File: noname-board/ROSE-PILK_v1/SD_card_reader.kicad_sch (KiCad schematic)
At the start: 1 part, among them J5 Conn_02x08_Odd_Even

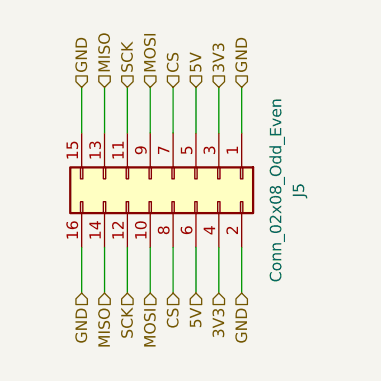
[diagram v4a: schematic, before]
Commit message: schematic finished, placement progress
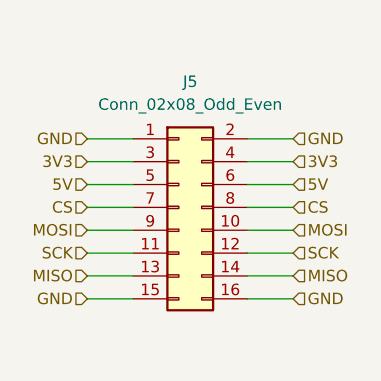
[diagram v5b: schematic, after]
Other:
- moved on the sheet: J5
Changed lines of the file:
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@@
 (kicad_sch (version 20230121) (generator eeschema)
   (paper "A4")
-  (wire (pts (xy 126.365 130.175) (xy 126.365 135.255))
+  (wire (pts (xy 129.54 120.65) (xy 134.62 120.65))
     (stroke (width 0) (type default))
   )
-  (wire (pts (xy 123.825 112.395) (xy 123.825 117.475))
+  (wire (pts (xy 111.76 123.19) (xy 116.84 123.19))
     (stroke (width 0) (type default))
   )
-  (wire (pts (xy 128.905 130.175) (xy 128.905 135.255))
+  (wire (pts (xy 129.54 118.11) (xy 134.62 118.11))
     (stroke (width 0) (type default))
   )
-  (wire (pts (xy 123.825 130.175) (xy 123.825 135.255))
+  (wire (pts (xy 129.54 123.19) (xy 134.62 123.19))
     (stroke (width 0) (type default))
   )
-  (wire (pts (xy 113.665 130.175) (xy 113.665 135.255))
+  (wire (pts (xy 129.54 133.35) (xy 134.62 133.35))
     (stroke (width 0) (type default))
   )
-  (wire (pts (xy 116.205 112.395) (xy 116.205 117.475))
+  (wire (pts (xy 111.76 130.81) (xy 116.84 130.81))
     (stroke (width 0) (type default))
   )
-  (wire (pts (xy 121.285 130.175) (xy 121.285 135.255))
+  (wire (pts (xy 129.54 125.73) (xy 134.62 125.73))
     (stroke (width 0) (type default))
   )
-  (wire (pts (xy 116.205 130.175) (xy 116.205 135.255))
+  (wire (pts (xy 129.54 130.81) (xy 134.62 130.81))
     (stroke (width 0) (type default))
   )
-  (wire (pts (xy 118.745 130.175) (xy 118.745 135.255))
+  (wire (pts (xy 129.54 128.27) (xy 134.62 128.27))
     (stroke (width 0) (type default))
   )
-  (wire (pts (xy 111.125 130.175) (xy 111.125 135.255))
+  (wire (pts (xy 129.54 135.89) (xy 134.62 135.89))
     (stroke (width 0) (type default))
   )
-  (wire (pts (xy 113.665 112.395) (xy 113.665 117.475))
+  (wire (pts (xy 111.76 133.35) (xy 116.84 133.35))
     (stroke (width 0) (type default))
   )
-  (wire (pts (xy 118.745 112.395) (xy 118.745 117.475))
+  (wire (pts (xy 111.76 128.27) (xy 116.84 128.27))
     (stroke (width 0) (type default))
   )
-  (wire (pts (xy 128.905 112.395) (xy 128.905 117.475))
+  (wire (pts (xy 111.76 118.11) (xy 116.84 118.11))
     (stroke (width 0) (type default))
   )
-  (wire (pts (xy 121.285 112.395) (xy 121.285 117.475))
+  (wire (pts (xy 111.76 125.73) (xy 116.84 125.73))
     (stroke (width 0) (type default))
   )
-  (wire (pts (xy 126.365 112.395) (xy 126.365 117.475))
+  (wire (pts (xy 111.76 120.65) (xy 116.84 120.65))
     (stroke (width 0) (type default))
   )
-  (wire (pts (xy 111.125 112.395) (xy 111.125 117.475))
+  (wire (pts (xy 111.76 135.89) (xy 116.84 135.89))
     (stroke (width 0) (type default))
   )
-  (hierarchical_label "GND" (shape input) (at 111.125 112.395 90) (fields_autoplaced)
+  (hierarchical_label "GND" (shape input) (at 111.76 135.89 180) (fields_autoplaced)
+    (effects (font (size 1.27 1.27)) (justify right))
+  )
+  (hierarchical_label "GND" (shape input) (at 134.62 135.89 0) (fields_autoplaced)
     (effects (font (size 1.27 1.27)) (justify left))
   )
-  (hierarchical_label "GND" (shape input) (at 111.125 135.255 270) (fields_autoplaced)
+  (hierarchical_label "MISO" (shape input) (at 134.62 133.35 0) (fields_autoplaced)
+    (effects (font (size 1.27 1.27)) (justify left))
+  )
+  (hierarchical_label "MOSI" (shape input) (at 134.62 128.27 0) (fields_autoplaced)
+    (effects (font (size 1.27 1.27)) (justify left))
+  )
+  (hierarchical_label "SCK" (shape input) (at 134.62 130.81 0) (fields_autoplaced)
+    (effects (font (size 1.27 1.27)) (justify left))
+  )
+  (hierarchical_label "GND" (shape input) (at 111.76 118.11 180) (fields_autoplaced)
     (effects (font (size 1.27 1.27)) (justify right))
   )
-  (hierarchical_label "MISO" (shape input) (at 113.665 135.255 270) (fields_autoplaced)
+  (hierarchical_label "SCK" (shape input) (at 111.76 130.81 180) (fields_autoplaced)
     (effects (font (size 1.27 1.27)) (justify right))
   )
-  (hierarchical_label "MOSI" (shape input) (at 118.745 135.255 270) (fields_autoplaced)
+  (hierarchical_label "MISO" (shape input) (at 111.76 133.35 180) (fields_autoplaced)
     (effects (font (size 1.27 1.27)) (justify right))
   )
-  (hierarchical_label "SCK" (shape input) (at 116.205 135.255 270) (fields_autoplaced)
+  (hierarchical_label "3V3" (shape input) (at 134.62 120.65 0) (fields_autoplaced)
+    (effects (font (size 1.27 1.27)) (justify left))
+  )
+  (hierarchical_label "3V3" (shape input) (at 111.76 120.65 180) (fields_autoplaced)
     (effects (font (size 1.27 1.27)) (justify right))
   )
-  (hierarchical_label "GND" (shape input) (at 128.905 112.395 90) (fields_autoplaced)
+  (hierarchical_label "GND" (shape input) (at 134.62 118.11 0) (fields_autoplaced)
     (effects (font (size 1.27 1.27)) (justify left))
   )
-  (hierarchical_label "SCK" (shape input) (at 116.205 112.395 90) (fields_autoplaced)
+  (hierarchical_label "CS" (shape input) (at 111.76 125.73 180) (fields_autoplaced)
+    (effects (font (size 1.27 1.27)) (justify right))
+  )
+  (hierarchical_label "5V" (shape input) (at 134.62 123.19 0) (fields_autoplaced)
     (effects (font (size 1.27 1.27)) (justify left))
   )
-  (hierarchical_label "MISO" (shape input) (at 113.665 112.395 90) (fields_autoplaced)
+  (hierarchical_label "5V" (shape input) (at 111.76 123.19 180) (fields_autoplaced)
+    (effects (font (size 1.27 1.27)) (justify right))
+  )
+  (hierarchical_label "CS" (shape input) (at 134.62 125.73 0) (fields_autoplaced)
     (effects (font (size 1.27 1.27)) (justify left))
   )
-  (hierarchical_label "3V3" (shape input) (at 126.365 135.255 270) (fields_autoplaced)
+  (hierarchical_label "MOSI" (shape input) (at 111.76 128.27 180) (fields_autoplaced)
     (effects (font (size 1.27 1.27)) (justify right))
   )
-  (hierarchical_label "3V3" (shape input) (at 126.365 112.395 90) (fields_autoplaced)
-    (effects (font (size 1.27 1.27)) (justify left))
-  )
-  (hierarchical_label "GND" (shape input) (at 128.905 135.255 270) (fields_autoplaced)
-    (effects (font (size 1.27 1.27)) (justify right))
-  )
-  (hierarchical_label "CS" (shape input) (at 121.285 112.395 90) (fields_autoplaced)
-    (effects (font (size 1.27 1.27)) (justify left))
-  )
-  (hierarchical_label "5V" (shape input) (at 123.825 135.255 270) (fields_autoplaced)
-    (effects (font (size 1.27 1.27)) (justify right))
-  )
-  (hierarchical_label "5V" (shape input) (at 123.825 112.395 90) (fields_autoplaced)
-    (effects (font (size 1.27 1.27)) (justify left))
-  )
-  (hierarchical_label "CS" (shape input) (at 121.285 135.255 270) (fields_autoplaced)
-    (effects (font (size 1.27 1.27)) (justify right))
-  )
-  (hierarchical_label "MOSI" (shape input) (at 118.745 112.395 90) (fields_autoplaced)
-    (effects (font (size 1.27 1.27)) (justify left))
-  )
-  (symbol (lib_id "Connector_Generic:Conn_02x08_Odd_Even") (at 121.285 122.555 270) (unit 1)
+  (symbol (lib_id "Connector_Generic:Conn_02x08_Odd_Even") (at 121.92 125.73 0) (unit 1)
     (in_bom yes) (on_board yes) (dnp no) (fields_autoplaced)
-    (property "Reference" "J5" (at 135.255 123.825 0)
+    (property "Reference" "J5" (at 123.19 111.76 0)
       (effects (font (size 1.27 1.27)))
     )
-    (property "Value" "Conn_02x08_Odd_Even" (at 132.715 123.825 0)
+    (property "Value" "Conn_02x08_Odd_Even" (at 123.19 114.3 0)
       (effects (font (size 1.27 1.27)))
     )
-    (property "Footprint" "Connector_PinSocket_2.00mm:PinSocket_2x08_P2.00mm_Vertical" (at 121.285 122.555 0)
+    (property "Footprint" "Connector_PinSocket_2.00mm:PinSocket_2x08_P2.00mm_Vertical" (at 121.92 125.73 0)
       (effects (font (size 1.27 1.27)) hide)
     )
-    (property "Datasheet" "~" (at 121.285 122.555 0)
+    (property "Datasheet" "~" (at 121.92 125.73 0)
       (effects (font (size 1.27 1.27)) hide)
     )
